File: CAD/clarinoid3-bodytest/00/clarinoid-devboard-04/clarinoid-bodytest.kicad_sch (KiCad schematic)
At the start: 2 parts, among them U13 stereo pot w switch sub-board, U14 stereo pot subboard template

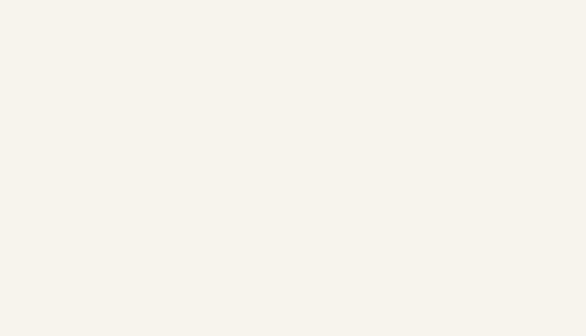
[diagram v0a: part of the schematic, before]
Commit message: adding a hardware layout sketch to the midi performer device PCB progress on the clarinoid3 body
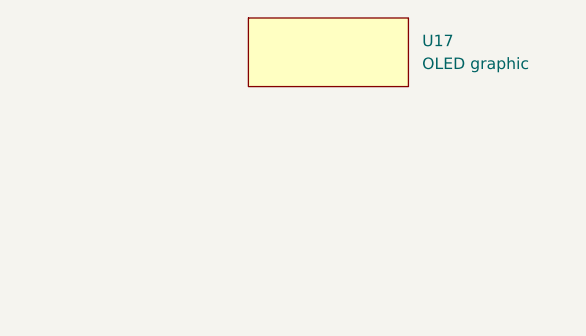
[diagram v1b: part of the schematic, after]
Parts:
- added U17: OLED graphic, clarinoid2:SSD1306_128x64_approximate, symbol clarinoid2:Placeholder
